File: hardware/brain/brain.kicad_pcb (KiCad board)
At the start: 4 copper layers, 120 x 80 mm, 113 parts, among them J1 QUADRANT 1, J10 POWER, J2 QUADRANT 2, J3 QUADRANT 3, J4 QUADRANT 4, J5 USB-C, J6 SWD, J7 ESP PROG, J8 PI ZERO, J9 MOTION, Q1 AO3401A, Q2 AO3400A, Q3 AO3400A, SW1 BOOT, SW2 RESET, SW3 ESP BOOT, SW4 ESP EN, SW5 USER, U1 STM32G474RE, U2 TPS62130, U3 AP2112K-3.3, U4 LP2985-5.0, U5 ESP32-S3-WROOM-1, U6 ADuM1201, U7 AMS1117-3.3, U8 74AHCT1G125, U9 USBLC6-2

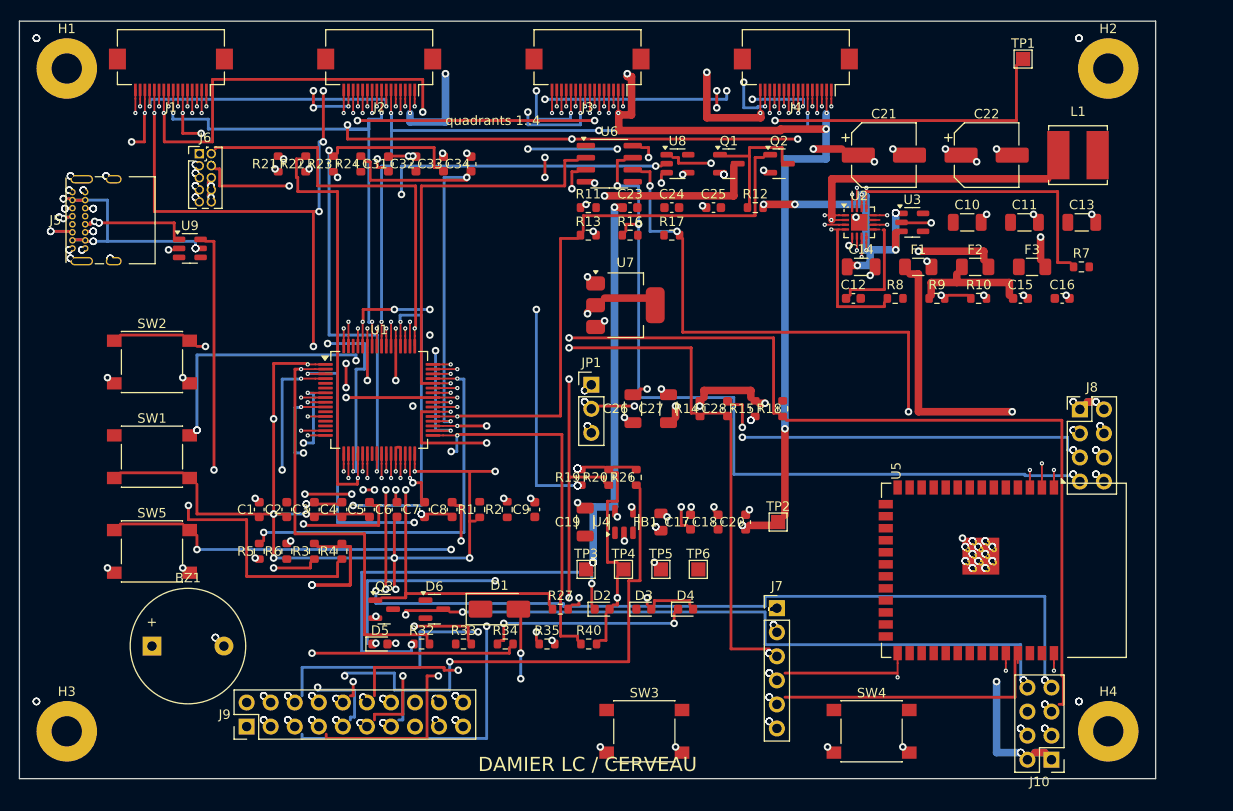
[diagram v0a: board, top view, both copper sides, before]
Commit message: Cerveau : build intermédiaire (module remonté, vias fusionnées)
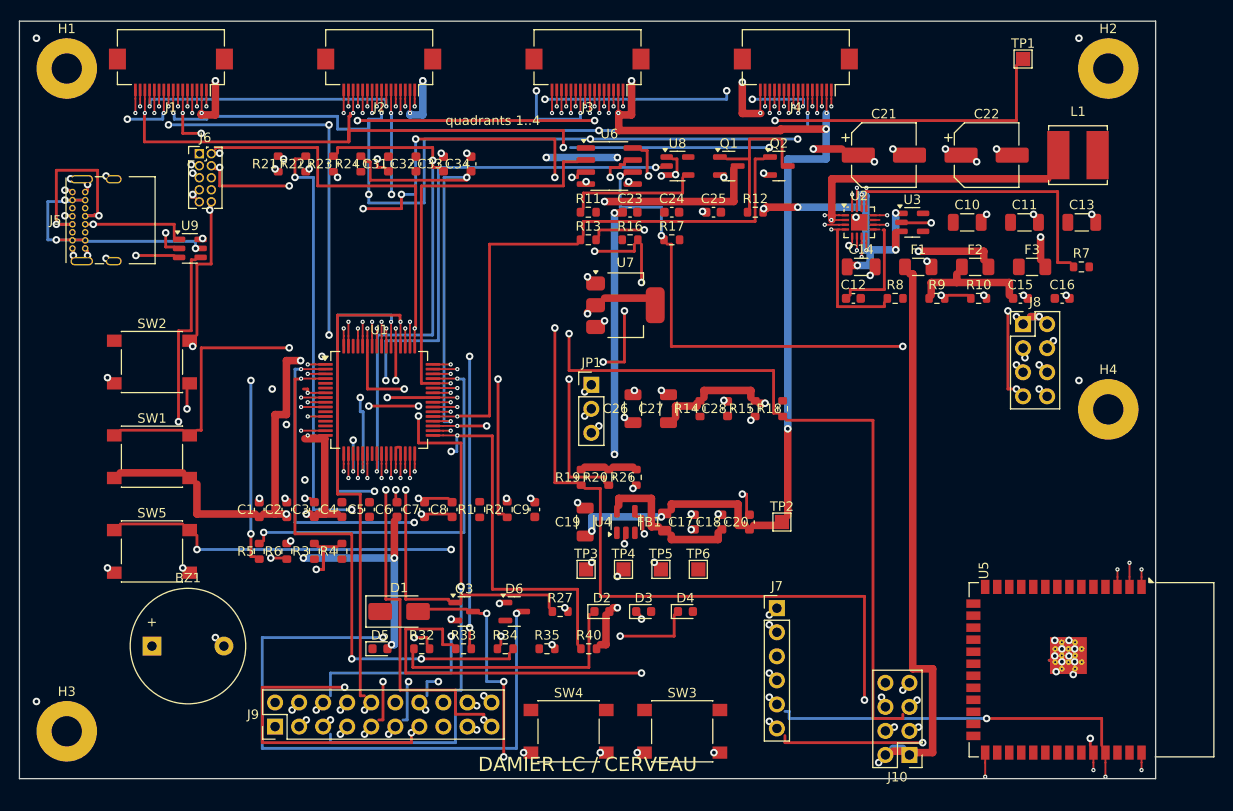
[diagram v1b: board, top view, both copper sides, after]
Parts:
- moved H4 34.0 mm to (115.0, 41.0)
- moved SW4 32.0 mm to (58.0, 75.0)
- moved J10 15.0 mm to (94.0, 77.5)
- moved U5 14.0 mm to (113.2, 68.5)
- moved J8 10.8 mm to (106.0, 32.0)
- moved D1 10.6 mm to (40.1, 62.4)
- moved Q3 8.45 mm to (47.0, 62.4)
- moved D6 8.44 mm to (52.3, 62.4)
- moved SW3 4.00 mm to (70.0, 75.0)
- moved J9 3.00 mm to (27.0, 74.5)
- moved D5 0.50 mm to (38.1, 66.3)
- moved R32 0.50 mm to (42.5, 66.3)
- moved R33 0.50 mm to (46.9, 66.3)
- moved R34 0.50 mm to (51.3, 66.3)
- moved R35 0.50 mm to (55.7, 66.3)
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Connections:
- J5 pad A8: SBU1 -> (no net)
- J5 pad B8: SBU2 -> (no net)
- J6 pad 6: NRST -> (no net)
- J6 pad 8: NRST -> (no net)
- R16 pad 1: COMM_TXD -> ESP_TXD
- R16 pad 2: ESP_RXD -> COMM_TXD
- R17 pad 1: ESP_TXD -> COMM_RXD
- R17 pad 2: COMM_RXD -> ESP_RXD
- U3 pad 4: 3V3_NC -> (no net)
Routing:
- net DAMP_EN_N: track 149.5 -> 9.58 mm, vias 9 -> 5
- net I2C_SDA: track 45.2 -> 133.4 mm, vias 9 -> 8
- net ESP_EN: track 79.0 -> 3.73 mm, vias 10 -> 2
- net PULSE_EN: track 77.5 -> 149.6 mm
- net MUX_EN_H: track 133.3 -> 62.4 mm, vias 12 -> 6
- net CC2: track 68.5 -> 0.00 mm, vias 4 -> 0
- net CC1: track 67.5 -> 0.00 mm, vias 3 -> 0
- net 3V3: track 164.4 -> 112.7 mm, vias 40 -> 17
- net ENDSTOP_X: track 86.5 -> 41.6 mm, vias 7 -> 2
- net USB_DP: track 0.00 -> 44.4 mm, vias 0 -> 2
- net LED3_K: track 0.00 -> 42.4 mm, vias 0 -> 2
- net BOOT0: track 30.8 -> 69.4 mm, vias 5 -> 3
- net USB_DP_C: track 0.00 -> 36.0 mm, vias 0 -> 3
- net CHG_STAT: track 96.1 -> 131.5 mm, vias 7 -> 3
- net 5VA: track 127.0 -> 161.3 mm
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
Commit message: Cerveau : build final ; résultats du DRC à jour (aucune erreur hors nets ouverts)
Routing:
- net ESP_RXD: track 36.0 -> 38.0 mm, vias 4 -> 2
- net VBAT_IN: track 57.8 -> 56.1 mm
- net ESP_TXD: track 39.6 -> 38.1 mm, vias 3 -> 2
- net ESP_IO0: track 66.9 -> 65.4 mm, vias 5 -> 4
- net GND: track 96.9 -> 96.0 mm
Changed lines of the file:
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@@
   (via (at 115.97 57.9) (size 0.45) (drill 0.2) (layers "F.Cu" "B.Cu") (net 19))
   (segment (start 102 77.25) (end 102 78.3) (width 0.2) (layer "F.Cu") (net 20))
-  (segment (start 102 78.3) (end 102 79.8) (width 0.2) (layer "F.Cu") (net 20))
-  (via (at 102 79.8) (size 0.45) (drill 0.2) (layers "F.Cu" "B.Cu") (net 20))
   (segment (start 113.43 77.25) (end 113.43 78.3) (width 0.2) (layer "F.Cu") (net 86))
   (segment (start 113.43 78.3) (end 113.43 79.1) (width 0.2) (layer "F.Cu") (net 86))
   (via (at 113.43 79.1) (size 0.45) (drill 0.2) (layers "F.Cu" "B.Cu") (net 86))
   (segment (start 114.7 77.25) (end 114.7 78.3) (width 0.2) (layer "F.Cu") (net 87))
-  (segment (start 114.7 78.3) (end 114.7 79.8) (width 0.2) (layer "F.Cu") (net 87))
-  (via (at 114.7 79.8) (size 0.45) (drill 0.2) (layers "F.Cu" "B.Cu") (net 87))
   (segment (start 118.51 77.25) (end 118.51 78.3) (width 0.2) (layer "F.Cu") (net 4))
   (segment (start 118.51 78.3) (end 118.51 79.1) (width 0.2) (layer "F.Cu") (net 4))
@@
   (segment (start 77.25 68.85) (end 79.2 68.85) (width 0.3) (layer "In2.Cu") (net 20))
   (via (at 79.2 68.85) (size 0.8) (drill 0.4) (layers "F.Cu" "B.Cu") (net 20))
-  (segment (start 113.1 76.5) (end 113.1 75.75) (width 0.3) (layer "F.Cu") (net 86))
-  (segment (start 113.1 75.75) (end 95.4 75.75) (width 0.3) (layer "In2.Cu") (net 86))
-  (segment (start 95.4 75.75) (end 95.4 76.2) (width 0.3) (layer "In2.Cu") (net 86))
-  (segment (start 95.4 76.2) (end 80.85 76.2) (width 0.3) (layer "F.Cu") (net 86))
-  (segment (start 80.85 76.2) (end 80.85 75.45) (width 0.3) (layer "F.Cu") (net 86))
-  (via (at 113.1 75.75) (size 0.8) (drill 0.4) (layers "F.Cu" "B.Cu") (net 86))
-  (via (at 95.4 76.2) (size 0.8) (drill 0.4) (layers "F.Cu" "B.Cu") (net 86))
+  (segment (start 113.4 78.75) (end 102.3 78.75) (width 0.3) (layer "F.Cu") (net 86))
+  (segment (start 102.3 78.75) (end 102.3 78.9) (width 0.3) (layer "F.Cu") (net 86))
+  (segment (start 102.3 78.9) (end 80.85 78.9) (width 0.3) (layer "F.Cu") (net 86))
+  (segment (start 80.85 78.9) (end 80.85 75.45) (width 0.3) (layer "F.Cu") (net 86))
   (via (at 79.2 73.95) (size 0.8) (drill 0.4) (layers "F.Cu" "B.Cu") (net 86))
   (segment (start 30.45 40.2) (end 31.05 40.2) (width 0.3) (layer "In1.Cu") (net 48))
@@
   (segment (start 94.05 26.7) (end 94.35 26.7) (width 0.8) (layer "F.Cu") (net 56))
   (segment (start 94.35 26.7) (end 94.35 68.4) (width 0.8) (layer "F.Cu") (net 56))
-  (segment (start 94.35 68.4) (end 96.45 68.4) (width 0.8) (layer "F.Cu") (net 56))
-  (segment (start 96.45 68.4) (end 96.45 77.25) (width 0.8) (layer "F.Cu") (net 56))
-  (segment (start 96.45 77.25) (end 94.8 77.25) (width 0.8) (layer "F.Cu") (net 56))
-  (segment (start 93.3 77.1) (end 92.25 77.1) (width 0.8) (layer "F.Cu") (net 56))
-  (via (at 90.75 78.3) (size 0.8) (drill 0.4) (layers "F.Cu" "B.Cu") (net 56))
+  (segment (start 94.35 68.4) (end 95.85 68.4) (width 0.8) (layer "F.Cu") (net 56))
+  (segment (start 95.85 68.4) (end 95.85 76.8) (width 0.8) (layer "F.Cu") (net 56))
+  (segment (start 95.85 76.8) (end 94.8 76.8) (width 0.8) (layer "F.Cu") (net 56))
+  (segment (start 93.3 76.8) (end 92.25 76.8) (width 0.8) (layer "F.Cu") (net 56))
+  (via (at 92.25 76.8) (size 0.8) (drill 0.4) (layers "F.Cu" "B.Cu") (net 56))
   (segment (start 93.3 76.8) (end 92.25 76.8) (width 0.8) (layer "In2.Cu") (net 56))
   (segment (start 93.3 76.8) (end 92.25 76.8) (width 0.8) (layer "B.Cu") (net 56))
@@
   (segment (start 48.15 72.3) (end 48.3 72.3) (width 0.3) (layer "In2.Cu") (net 4))
   (segment (start 48.15 72.3) (end 48.3 72.3) (width 0.3) (layer "B.Cu") (net 4))
-  (segment (start 94.8 74.55) (end 94.95 74.55) (width 0.3) (layer "F.Cu") (net 4))
-  (via (at 94.95 74.55) (size 0.8) (drill 0.4) (layers "F.Cu" "B.Cu") (net 4))
-  (segment (start 94.8 74.55) (end 94.95 74.55) (width 0.3) (layer "In2.Cu") (net 4))
-  (segment (start 94.8 74.55) (end 94.95 74.55) (width 0.3) (layer "B.Cu") (net 4))
-  (segment (start 92.25 74.55) (end 92.4 74.55) (width 0.3) (layer "F.Cu") (net 4))
-  (via (at 92.4 74.55) (size 0.8) (drill 0.4) (layers "F.Cu" "B.Cu") (net 4))
-  (segment (start 92.25 74.55) (end 92.4 74.55) (width 0.3) (layer "In2.Cu") (net 4))
-  (segment (start 92.25 74.55) (end 92.4 74.55) (width 0.3) (layer "B.Cu") (net 4))
+  (via (at 93.3 75.75) (size 0.8) (drill 0.4) (layers "F.Cu" "B.Cu") (net 4))
+  (via (at 92.25 75.75) (size 0.8) (drill 0.4) (layers "F.Cu" "B.Cu") (net 4))
   (via (at 45.6 63.15) (size 0.8) (drill 0.4) (layers "F.Cu" "B.Cu") (net 4))
   (via (at 57.6 61.95) (size 0.8) (drill 0.4) (layers "F.Cu" "B.Cu") (net 4))

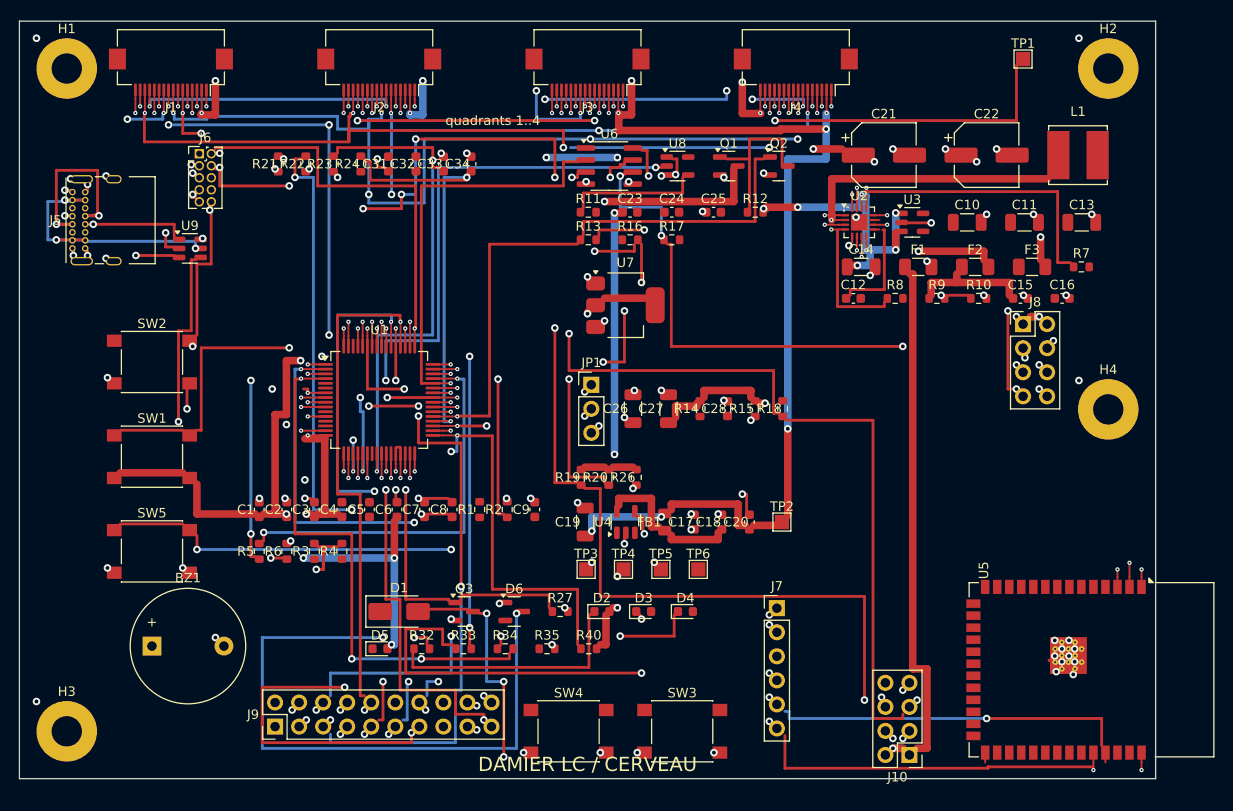
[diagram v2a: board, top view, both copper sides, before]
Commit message: Cerveau fermé : haul VBAT, nets de liaison en premier, rip-up et reroutage, gerbers ; 4 x 4 régénéré et diagnostiqué
boardgen : rip-up et reroutage des nets murés à la fin du routage
(GenericBoard.reroute_walled) : un net en morceaux à la fois, ses
voisins à moins de 0,6 mm soulevés avec lui et reroutés, la levée
gardée si moins de nets restent en morceaux ; chaque piste et via se
souvient des lignes écrites dans le fichier de carte pour être levée ;
journal des levées imprimé par le build, BOARDGEN_RIP_UP=0 pour
comparer.

Cerveau : haul VBAT dessiné à la main sur la face arrière (bord sud,
colonne à l'ouest du lien puissance, montée au fusible F1) ; VBAT,
les quatre sorties analogiques et les deux lignes UART de l'isolateur
routés en premier ; chaque LED d'état à côté de sa résistance.
Résultat : 0 net ouvert, DRC KiCad sans élément non connecté ni
erreur, brain-gerbers.zip et empreinte commités, image régénérée.

Quadrant 4 x 4 : build du 20/09 commité (47 nets ouverts, 52 éléments
non connectés), diagnostic des trois champs d'échappées (multiplexeurs
LFCSP face à face, décodeurs à une rangée de vias, colonne
d'amplification) et plan des éventails à la main dans la note 04 ;
README, notes 07, 09 et 23 à jour.

Tests : l'archive du cerveau est attendue par les tests de gerbers et
par l'audit de fabrication.
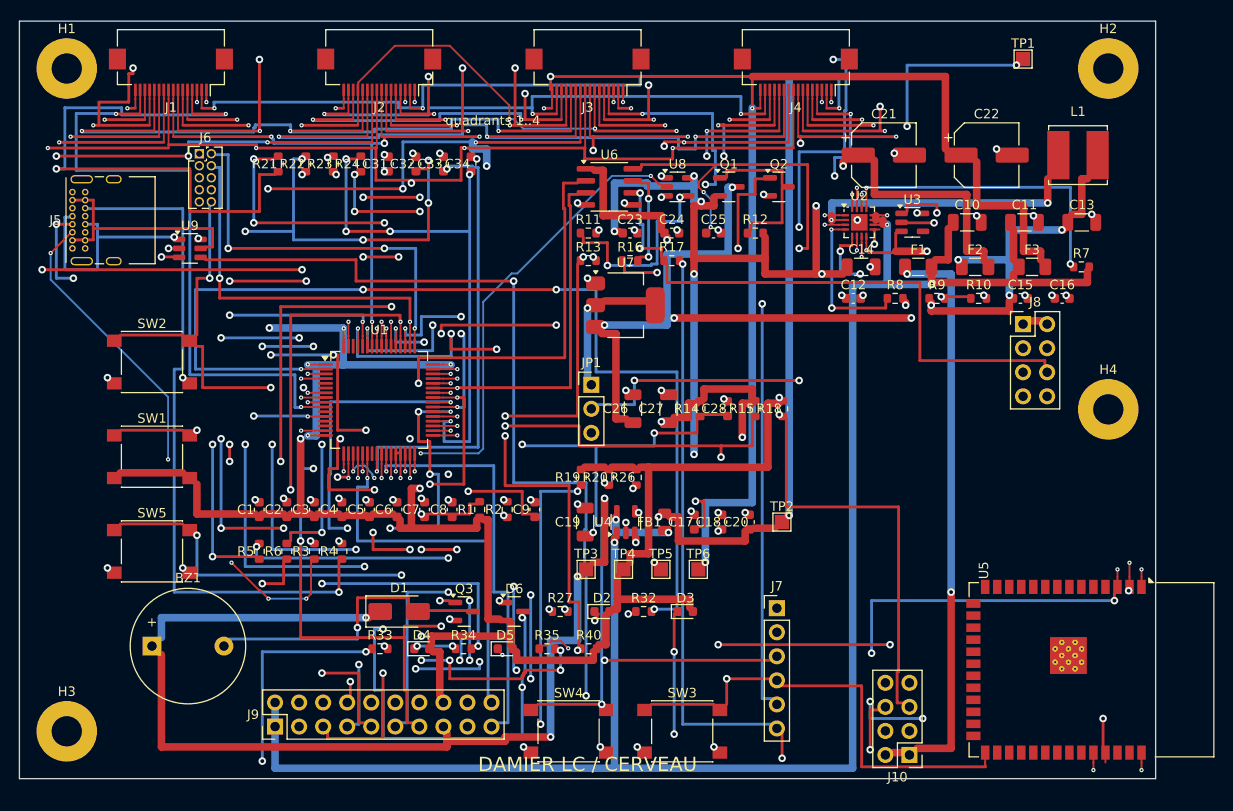
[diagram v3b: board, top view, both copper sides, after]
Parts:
- moved D4 28.1 mm to (42.5, 66.3)
- moved R32 23.8 mm to (65.9, 62.4)
- moved D5 13.2 mm to (51.3, 66.3)
- moved R33 8.82 mm to (38.1, 66.3)
- moved R34 4.41 mm to (46.9, 66.3)
- moved D3 4.41 mm to (70.3, 62.4)
- moved C23 2.20 mm to (64.5, 22.4)
- moved C24 2.20 mm to (68.9, 22.4)
- moved C25 2.20 mm to (73.3, 22.4)
- moved Q1 2.20 mm to (74.9, 17.5)
- moved Q2 2.20 mm to (80.2, 17.5)
- moved R11 2.20 mm to (60.1, 22.4)
- moved R12 2.20 mm to (77.7, 22.4)
- moved R13 2.20 mm to (60.1, 25.3)
- moved R16 2.20 mm to (64.5, 25.3)
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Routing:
- net 3V3: track 112.7 -> 430.6 mm
- net VBAT: track 9.81 -> 193.8 mm, vias 3 -> 5
- net 5V: track 92.2 -> 276.1 mm, vias 11 -> 20
- net MUX_EN_L: track 9.58 -> 162.6 mm
- net DAMP_EN_N: track 9.58 -> 153.9 mm
- net ESP_EN: track 3.73 -> 129.9 mm, vias 2 -> 8
- net LED_DIN1: track 1.75 -> 127.8 mm, vias 1 -> 5
- net VIN: track 60.7 -> 184.9 mm, vias 8 -> 6
- net USB_DP: track 44.4 -> 147.3 mm, vias 2 -> 3
- net MUX_EN_H: track 62.4 -> 157.1 mm
- net AMP_OUT2: track 16.0 -> 108.7 mm, vias 2 -> 5
- net CC2: track 0.00 -> 72.0 mm, vias 0 -> 1
- net AMP_OUT4: track 2.45 -> 73.0 mm, vias 1 -> 5
- net LED_STAT1: track 46.2 -> 109.1 mm, vias 3 -> 4
- net ESP_TXD: track 38.1 -> 100.9 mm, vias 2 -> 5
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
